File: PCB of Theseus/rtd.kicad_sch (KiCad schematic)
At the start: 13 parts, among them J3 Screw_Terminal_01x06, U3 REF200, U4 INA326, U5 INA326, U7 REF200

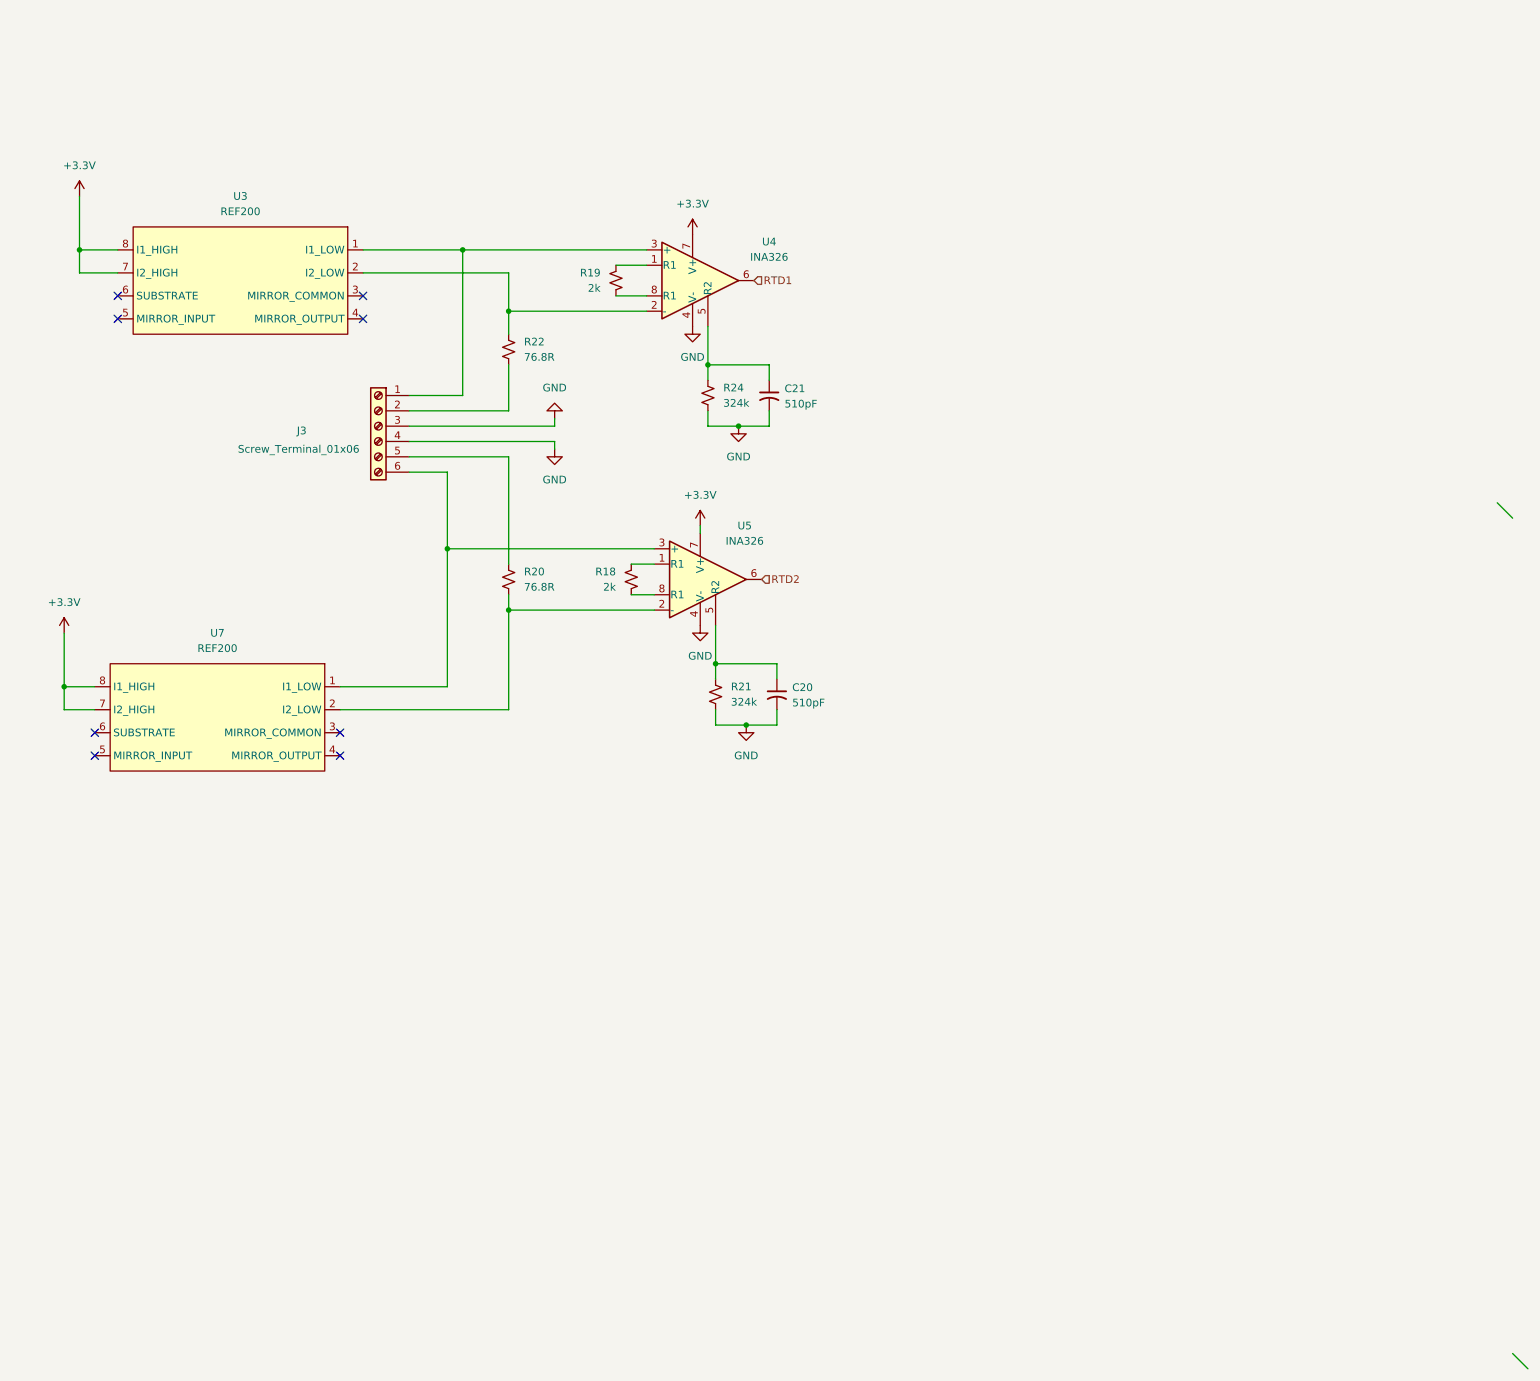
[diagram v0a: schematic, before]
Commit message: Updates to schematic, added 3rd RTD, initial PCB layout completed.
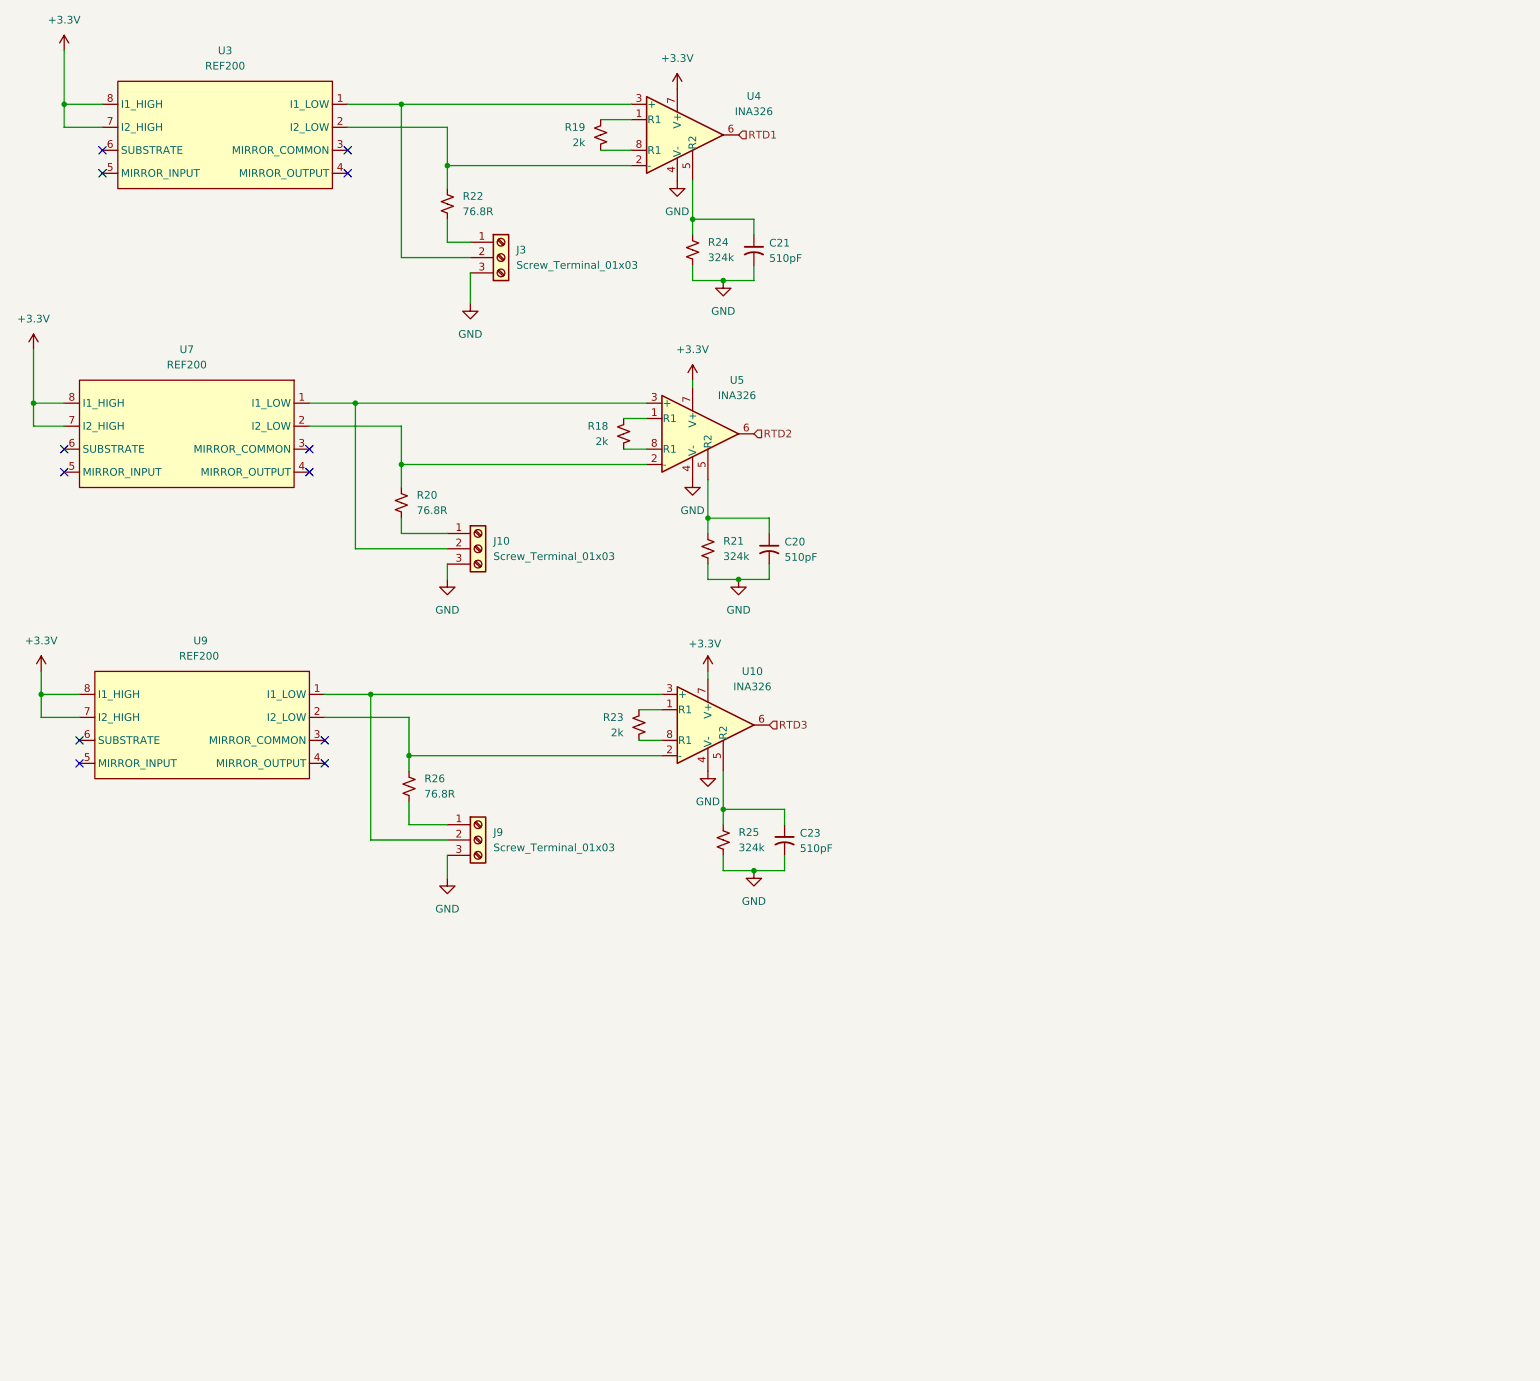
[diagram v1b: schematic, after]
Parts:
- removed J3: Screw_Terminal_01x06, symbol Connector:Screw_Terminal_01x06
- added C23: 510pF, Capacitor_SMD:C_0201_0603Metric_Pad0.64x0.40mm_HandSolder, symbol Device:C_Small_US
- added J10, J3, J9: Screw_Terminal_01x03, TerminalBlock_CUI:TerminalBlock_CUI_TB007-508-03_1x03_P5.08mm_Horizontal, symbol Connector:Screw_Terminal_01x03
- added R23: 2k, Resistor_SMD:R_0603_1608Metric_Pad0.98x0.95mm_HandSolder, symbol Device:R_Small_US
- added R25: 324k, Resistor_SMD:R_0201_0603Metric_Pad0.64x0.40mm_HandSolder, symbol Device:R_Small_US
- added R26: 76.8R, Resistor_SMD:R_0603_1608Metric_Pad0.98x0.95mm_HandSolder, symbol Device:R_Small_US
- added U10: INA326, Package_SO:MSOP-8_3x3mm_P0.65mm, symbol Amplifier_Instrumentation:INA326
- added U9: REF200, Package_SO:SOIC-8_3.9x4.9mm_P1.27mm, symbol FYDP_Library:REF200
- C20, C21: footprint (none) -> Capacitor_SMD:C_0201_0603Metric_Pad0.64x0.40mm_HandSolder
- R18, R19, R20, R22: footprint (none) -> Resistor_SMD:R_0603_1608Metric_Pad0.98x0.95mm_HandSolder
- R21, R24: footprint (none) -> Resistor_SMD:R_0201_0603Metric_Pad0.64x0.40mm_HandSolder
- U3, U7: footprint (none) -> Package_SO:SOIC-8_3.9x4.9mm_P1.27mm
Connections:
- net +3.3V: now also U10.7 (V+), U9.7 (I2_HIGH), U9.8 (I1_HIGH)
- net GND: now also C23.2, J10.3 (Pin_3), J3.3 (Pin_3), J9.3 (Pin_3), R25.2, U10.4 (V-)
- net at U3.1 (I1_LOW), U4.3 (+): now also J3.2 (Pin_2)
- net at U5.2 (-), U7.2 (I2_LOW): now also R20.1; no longer R20.2
- net at U5.3 (+), U7.1 (I1_LOW): now also J10.2 (Pin_2)
- net at R22.2: now also J3.1 (Pin_1)
- new net: J9.2 (Pin_2), U10.3 (+), U9.1 (I1_LOW)
- new net: R26.1, U10.2 (-), U9.2 (I2_LOW)
- new net: R23.1, U10.1 (R1)
- new net: R23.2, U10.8 (R1)
- new net: C23.1, R25.1, U10.5 (R2)
- new net: J10.1 (Pin_1), R20.2
- new net: J9.1 (Pin_1), R26.2
- new net RTD3: U10.6
- no-connect marks 8 -> 12
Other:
- moved on the sheet: C20, C21, R18, R19, R20, R21, R22, R24, U3, U4, U5, U7
